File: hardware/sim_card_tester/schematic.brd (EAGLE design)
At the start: 160 x 100 mm, 139 parts, among them IC1 TPS6300, J13 U.FL-R-SMT, J2 MICRO_USB_B_HIROSE_ZX62R-B-5P, J3 CON_MICRO_SDDM3AT-SF-PEJM5, J4 NANO_SIM, J5 NANO_SIM, J6 TC2030-JLINK-NL, J7 NANO_SIM, J8 NANO_SIM, Q1 MOSFET-NCHANNELSMD, Q2 MOSFET-NCHANNELSMD, Q6 MOSFET-NCHANNELSMD, Q7 SI223DDS, U1 AB1815-T3, U10 SIP32510, U11 SIP32510, U12 UBLOX_SARA_G350, U13 TXB0104RUT, U15 MAX4734EUB+, U2 BGA725L6-ALT, U20 MAX4734EUB+, U21 MAX4734EUB+, U22 MAX4734EUB+, U3 FTDI234XD, U4 SAFFB1G56KB0F0A, U5 MAX8887EZK33+T, U6 MCP73831, U7 MAX-M8, U8 MAX67XXMAX6749MAX67XX, U9 NRF52840, X1 ABS07-32.768KHZ-7-T, X4 32MHz, X5 32.768kHz

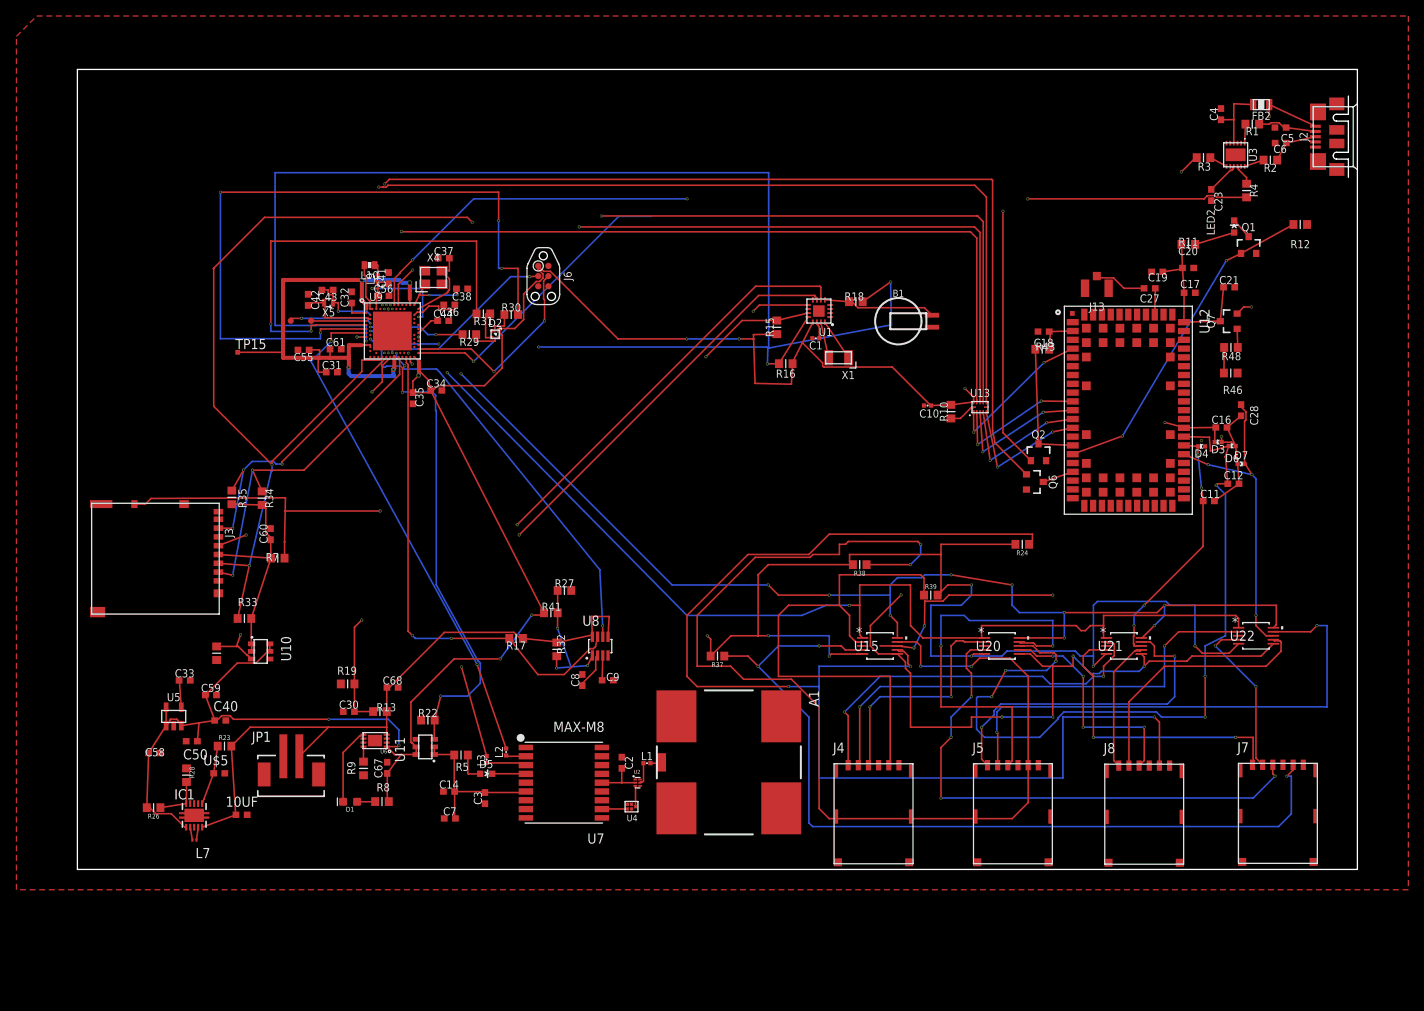
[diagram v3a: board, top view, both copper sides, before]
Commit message: fixed via and pad problem
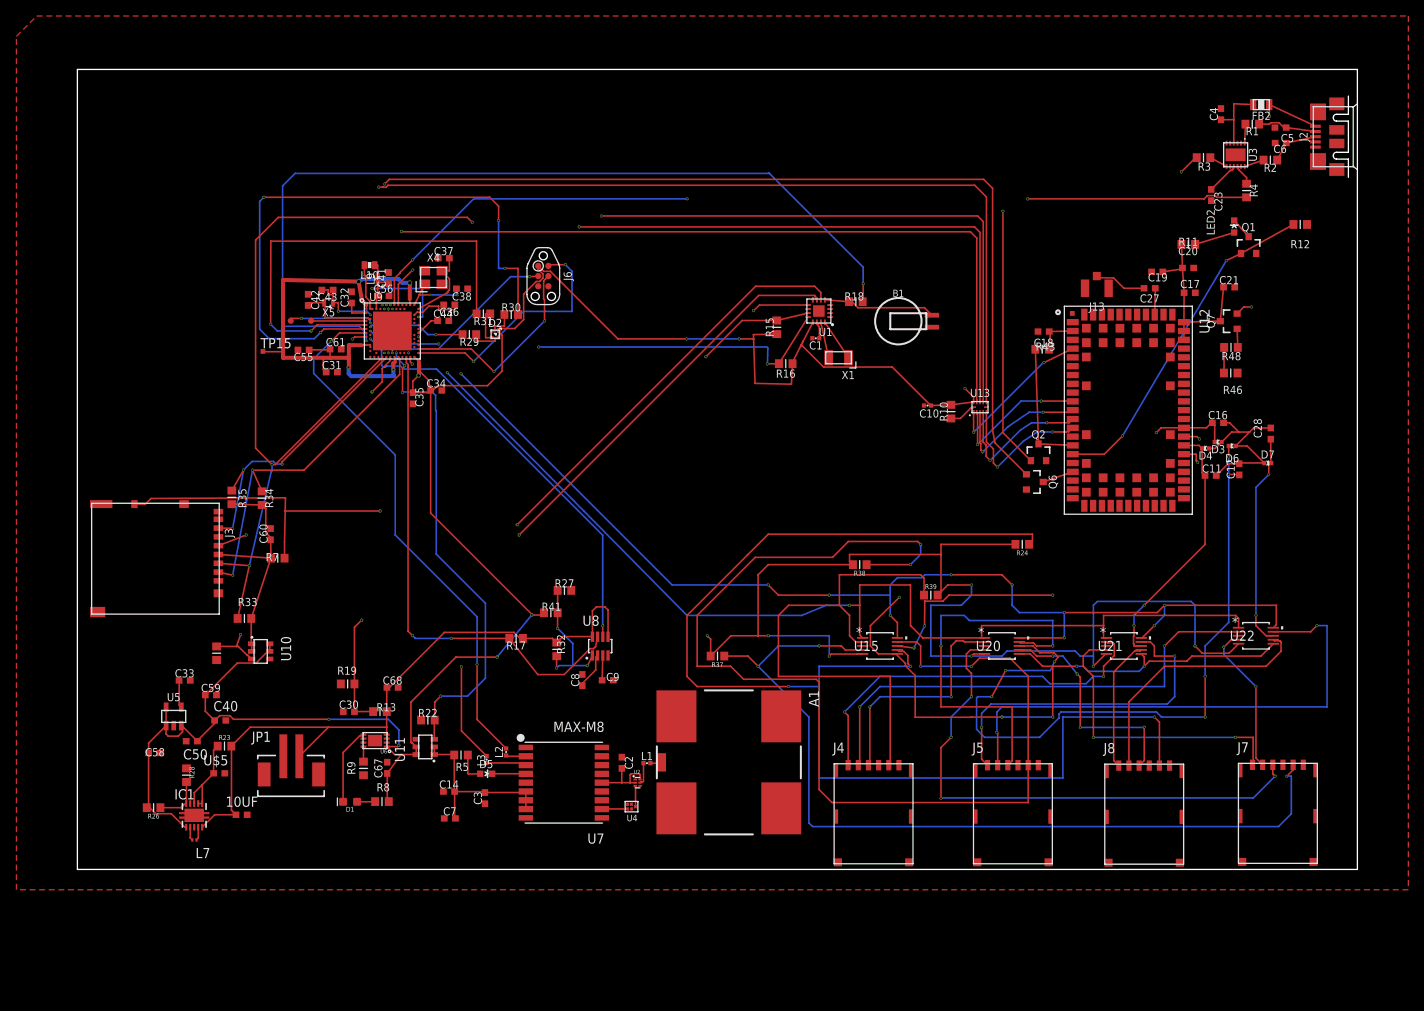
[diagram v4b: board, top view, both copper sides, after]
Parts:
- moved C28 4.72 mm to (149.2, 54.5), turned to 90 degrees
- moved D7 3.33 mm to (148.8, 50.8)
- moved C11 3.18 mm to (141.7, 49.2)
- moved TP15 3.15 mm to (23.2, 64.7)
- moved C12 1.95 mm to (145.2, 50.0), turned to 90 degrees
- moved C16 0.73 mm to (142.6, 55.8)
- moved D4 0.57 mm to (141.0, 52.6)
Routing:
- net !RTC_CS: track 202.4 -> 172.7 mm
- net LED_NRF_GREEN: track 90.3 -> 76.8 mm
- net NRF_MOSI: track 154.0 -> 147.3 mm
- net NRF_SWDIO: track 37.1 -> 30.6 mm, vias 1 -> 2
- net N$71: track 18.6 -> 24.8 mm, vias 2 -> 0
- net VCC: track 171.6 -> 166.8 mm
- net N$29: track 7.48 -> 11.3 mm
- net GPS_TXD: track 63.3 -> 66.6 mm
- net VCC_RF: track 5.96 -> 8.90 mm
- net MUX_EN: track 206.6 -> 208.9 mm
- net BAT: track 82.1 -> 84.5 mm
- net GSM_GATED: track 21.1 -> 23.3 mm
- net GPS_VCC: track 20.5 -> 22.7 mm
- net VCC2: track 141.4 -> 139.6 mm
- net GPS_PWR_EN: track 58.5 -> 60.1 mm, vias 3 -> 4
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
